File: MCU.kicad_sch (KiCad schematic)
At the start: 44 parts, among them SW201 RKB2SJM250SMTR LFS, SW202 RKB2SJM250SMTR LFS, U201 STM32F411RETx, Y201 24MHz

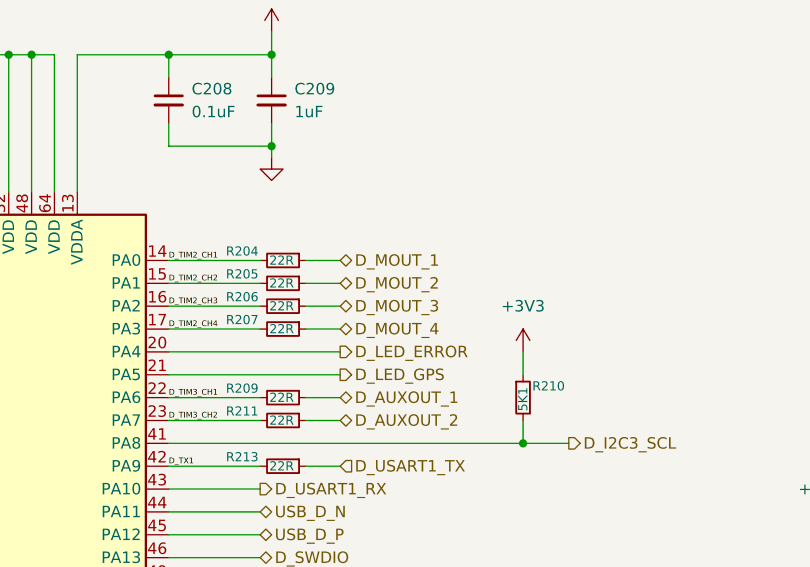
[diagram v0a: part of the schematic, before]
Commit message: fix: repositioned R24 - R206 & add silk screen for 5V input
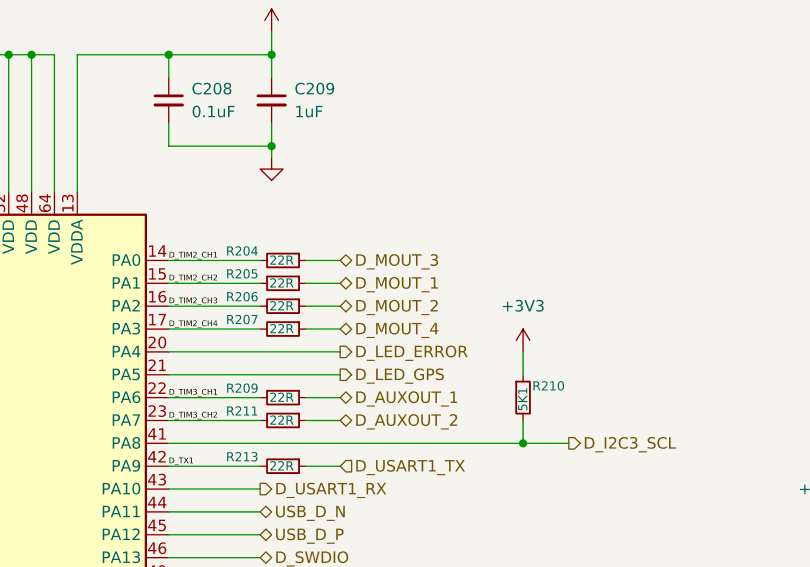
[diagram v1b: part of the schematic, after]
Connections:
- net D_MOUT_1: now also R205.1; no longer R204.1
- net D_MOUT_2: now also R206.1; no longer R205.1
- net D_MOUT_3: now also R204.1; no longer R206.1
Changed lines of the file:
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@@
 	(hierarchical_label "D_MOUT_2"
 		(shape bidirectional)
-		(at 182.88 72.39 0)
+		(at 182.88 74.93 0)
 		(effects
 			(font
@@
 	(hierarchical_label "D_MOUT_3"
 		(shape bidirectional)
-		(at 182.88 74.93 0)
+		(at 182.88 69.85 0)
 		(effects
 			(font
@@
 	(hierarchical_label "D_MOUT_1"
 		(shape bidirectional)
-		(at 182.88 69.85 0)
-		(effects
-			(font
+		(at 182.88 72.39 0)
+		(effects
+			(font

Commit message: fix: fix magnetometer pinout
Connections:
- net D_I2C1_SCL: now also U201.58 (PB6); no longer U201.61 (PB8)
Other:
- moved on the sheet: R221, R222
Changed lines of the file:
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@@
 	(title_block
 		(title "Udayate")
-		(date "2025-08-24")
-		(rev "1")
+		(date "2025-10-04")
+		(rev "1.1")
 		(comment 2 "LICENSE: CERN-OHL-S-2.0")
 		(comment 3 "GitHub: https://github.com/Ozonised/Udayate")
@@
 	)
 	(junction
-		(at 207.01 133.35)
+		(at 113.03 146.05)
 		(diameter 0)
 		(color 0 0 0 0)
 	)
 	(junction
-		(at 113.03 146.05)
+		(at 86.36 46.99)
 		(diameter 0)
 		(color 0 0 0 0)
 	)
 	(junction
-		(at 86.36 46.99)
+		(at 53.34 69.85)
 		(diameter 0)
 		(color 0 0 0 0)
 	)
 	(junction
-		(at 53.34 69.85)
+		(at 207.01 128.27)
 		(diameter 0)
 		(color 0 0 0 0)
@@
 	)
 	(junction
-		(at 210.82 120.65)
+		(at 210.82 118.11)
 		(diameter 0)
 		(color 0 0 0 0)
@@
 	)
 	(no_connect
-		(at 163.83 128.27)
-	)
-	(no_connect
 		(at 163.83 123.19)
 	)
@@
 	)
 	(no_connect
+		(at 163.83 133.35)
+	)
+	(no_connect
 		(at 128.27 87.63)
 	)
@@
 	(wire
 		(pts
-			(xy 214.63 123.19) (xy 214.63 120.65)
+			(xy 214.63 120.65) (xy 214.63 118.11)
 		)
 		(stroke
@@
 	(wire
 		(pts
-			(xy 210.82 120.65) (xy 214.63 120.65)
+			(xy 210.82 118.11) (xy 214.63 118.11)
 		)
 		(stroke
@@
 	(wire
 		(pts
-			(xy 214.63 128.27) (xy 214.63 130.81)
+			(xy 214.63 125.73) (xy 214.63 130.81)
 		)
 		(stroke
@@
 	(wire
 		(pts
-			(xy 210.82 119.38) (xy 210.82 120.65)
+			(xy 210.82 116.84) (xy 210.82 118.11)
 		)
 		(stroke
@@
 	(wire
 		(pts
-			(xy 163.83 82.55) (xy 182.88 82.55)
-		)
-		(stroke
-			(width 0)
-			(type default)
-		)
-	)
-	(wire
-		(pts
-			(xy 97.79 57.15) (xy 109.22 57.15)
+			(xy 163.83 128.27) (xy 207.01 128.27)
 		)
 		(stroke
@@
 	(wire
 		(pts
-			(xy 163.83 46.99) (xy 175.26 46.99)
+			(xy 163.83 82.55) (xy 182.88 82.55)
 		)
 		(stroke
@@
 	(wire
 		(pts
-			(xy 92.71 80.01) (xy 92.71 82.55)
+			(xy 97.79 57.15) (xy 109.22 57.15)
 		)
 		(stroke
@@
 	(wire
 		(pts
-			(xy 207.01 133.35) (xy 218.44 133.35)
+			(xy 163.83 46.99) (xy 175.26 46.99)
 		)
 		(stroke
@@
 	(wire
 		(pts
-			(xy 163.83 133.35) (xy 207.01 133.35)
+			(xy 92.71 80.01) (xy 92.71 82.55)
 		)
 		(stroke
@@
 	(wire
 		(pts
+			(xy 207.01 128.27) (xy 218.44 128.27)
+		)
+		(stroke
+			(width 0)
+			(type default)
+		)
+	)
+	(wire
+		(pts
 			(xy 203.2 87.63) (xy 203.2 90.17)
 		)
@@
 	(wire
 		(pts
-			(xy 207.01 120.65) (xy 207.01 123.19)
+			(xy 207.01 118.11) (xy 207.01 120.65)
 		)
 		(stroke
@@
 	(wire
 		(pts
-			(xy 163.83 72.39) (xy 173.99 72.39)
+			(xy 207.01 125.73) (xy 207.01 128.27)
 		)
 		(stroke
@@
 	(wire
 		(pts
-			(xy 121.92 118.11) (xy 128.27 118.11)
+			(xy 163.83 72.39) (xy 173.99 72.39)
 		)
 		(stroke
@@
 	(wire
 		(pts
-			(xy 99.06 87.63) (xy 104.14 87.63)
+			(xy 121.92 118.11) (xy 128.27 118.11)
 		)
 		(stroke
@@
 	(wire
 		(pts
-			(xy 153.67 46.99) (xy 153.67 62.23)
+			(xy 99.06 87.63) (xy 104.14 87.63)
 		)
 		(stroke
@@
 	(wire
 		(pts
-			(xy 113.03 146.05) (xy 118.11 146.05)
+			(xy 153.67 46.99) (xy 153.67 62.23)
 		)
 		(stroke
@@
 	(wire
 		(pts
-			(xy 207.01 128.27) (xy 207.01 133.35)
+			(xy 113.03 146.05) (xy 118.11 146.05)
 		)
 		(stroke
@@
 	(wire
 		(pts
-			(xy 207.01 120.65) (xy 210.82 120.65)
+			(xy 207.01 118.11) (xy 210.82 118.11)
 		)
 		(stroke
@@
 	(hierarchical_label "D_I2C1_SCL"
 		(shape output)
-		(at 218.44 133.35 0)
+		(at 218.44 128.27 0)
 		(effects
 			(font
@@
 	(symbol
 		(lib_id "power:+3V3")
-		(at 210.82 119.38 0)
+		(at 210.82 116.84 0)
 		(unit 1)
 		(exclude_from_sim no)
@@
 		(dnp no)
 		(property "Reference" "#PWR0214"
-			(at 210.82 123.19 0)
+			(at 210.82 120.65 0)
 			(effects
 				(font
@@
 		)
 		(property "Value" "+3V3"
-			(at 210.058 115.57 0)
+			(at 210.058 113.03 0)
 			(effects
 				(font
@@
 		)
 		(property "Footprint" ""
-			(at 210.82 119.38 0)
+			(at 210.82 116.84 0)
 			(effects
 				(font
@@
 		)
 		(property "Datasheet" ""
-			(at 210.82 119.38 0)
+			(at 210.82 116.84 0)
 			(effects
 				(font
@@
 		)
 		(property "Description" "Power symbol creates a global label with name \"+3V3\""
-			(at 210.82 119.38 0)
+			(at 210.82 116.84 0)
 			(effects
 				(font
@@
 	(symbol
 		(lib_id "Device:R_Small")
-		(at 214.63 125.73 0)
+		(at 214.63 123.19 0)
 		(unit 1)
 		(exclude_from_sim no)
@@
 		(dnp no)
 		(property "Reference" "R222"
-			(at 215.646 124.46 0)
+			(at 215.646 121.92 0)
 			(effects
 				(font
@@
 		)
 		(property "Value" "5K1"
-			(at 214.63 127.254 90)
+			(at 214.63 124.714 90)
 			(effects
 				(font
@@
 		)
 		(property "Footprint" "Resistor_SMD:R_0603_1608Metric_Pad0.98x0.95mm_HandSolder"
-			(at 214.63 125.73 0)
+			(at 214.63 123.19 0)
 			(effects
 				(font
@@
 		)
 		(property "Datasheet" "~"
-			(at 214.63 125.73 0)
+			(at 214.63 123.19 0)
 			(effects
 				(font
@@
 		)
 		(property "Description" "Resistor, small symbol"
-			(at 214.63 125.73 0)
+			(at 214.63 123.19 0)
 			(effects
 				(font
@@
 		)
 		(property "MPN" "CR0603-FX-5101ELF"
-			(at 214.63 125.73 0)
+			(at 214.63 123.19 0)
 			(effects
 				(font
@@
 		)
 		(property "Manufacturer" "Bourns"
-			(at 214.63 125.73 0)
+			(at 214.63 123.19 0)
 			(effects
 				(font
@@
 	(symbol
 		(lib_id "Device:R_Small")
-		(at 207.01 125.73 0)
+		(at 207.01 123.19 0)
 		(unit 1)
 		(exclude_from_sim no)
@@
 		(dnp no)
 		(property "Reference" "R221"
-			(at 208.026 124.46 0)
+			(at 208.026 121.92 0)
 			(effects
 				(font
@@
 		)
 		(property "Value" "5K1"
-			(at 207.01 127.254 90)
+			(at 207.01 124.714 90)
 			(effects
 				(font
@@
 		)
 		(property "Footprint" "Resistor_SMD:R_0603_1608Metric_Pad0.98x0.95mm_HandSolder"
-			(at 207.01 125.73 0)
+			(at 207.01 123.19 0)
 			(effects
 				(font
@@
 		)
 		(property "Datasheet" "~"
-			(at 207.01 125.73 0)
+			(at 207.01 123.19 0)
 			(effects
 				(font
@@
 		)
 		(property "Description" "Resistor, small symbol"
-			(at 207.01 125.73 0)
+			(at 207.01 123.19 0)
 			(effects
 				(font
@@
 		)
 		(property "MPN" "CR0603-FX-5101ELF"
-			(at 207.01 125.73 0)
+			(at 207.01 123.19 0)
 			(effects
 				(font
@@
 		)
 		(property "Manufacturer" "Bourns"
-			(at 207.01 125.73 0)
+			(at 207.01 123.19 0)
 			(effects
 				(font

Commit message: fix: EEPROM WC assigned to PC25
boot1 pull down, DFU now works
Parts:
- added R226: 5K1, Resistor_SMD:R_0603_1608Metric_Pad0.98x0.95mm_HandSolder, symbol Device:R_Small
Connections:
- net D_M24C02_WC: now also U201.25 (PC5); no longer U201.28 (PB2)
- net GND: now also R226.2
- new net D_BOOT1: R226.1, U201.28 (PB2)
- no-connect marks 15 -> 14
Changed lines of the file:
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@@
 	)
 	(no_connect
-		(at 128.27 105.41)
-	)
-	(no_connect
 		(at 128.27 100.33)
 	)
@@
 	(wire
 		(pts
+			(xy 208.28 104.14) (xy 208.28 105.41)
+		)
+		(stroke
+			(width 0)
+			(type default)
+		)
+	)
+	(wire
+		(pts
 			(xy 109.22 54.61) (xy 109.22 57.15)
 		)
@@
 	(wire
 		(pts
+			(xy 124.46 105.41) (xy 128.27 105.41)
+		)
+		(stroke
+			(width 0)
+			(type default)
+		)
+	)
+	(wire
+		(pts
 			(xy 210.82 118.11) (xy 214.63 118.11)
 		)
@@
 	(wire
 		(pts
+			(xy 196.85 104.14) (xy 200.66 104.14)
+		)
+		(stroke
+			(width 0)
+			(type default)
+		)
+	)
+	(wire
+		(pts
 			(xy 210.82 116.84) (xy 210.82 118.11)
 		)
@@
 	(wire
 		(pts
+			(xy 196.85 104.14) (xy 196.85 118.11)
+		)
+		(stroke
+			(width 0)
+			(type default)
+		)
+	)
+	(wire
+		(pts
 			(xy 104.14 86.36) (xy 104.14 87.63)
 		)
@@
 	(wire
 		(pts
-			(xy 163.83 118.11) (xy 181.61 118.11)
-		)
-		(stroke
-			(width 0)
-			(type default)
-		)
-	)
-	(wire
-		(pts
 			(xy 163.83 140.97) (xy 185.42 140.97)
 		)
@@
 	(wire
 		(pts
+			(xy 205.74 104.14) (xy 208.28 104.14)
+		)
+		(stroke
+			(width 0)
+			(type default)
+		)
+	)
+	(wire
+		(pts
 			(xy 87.63 121.92) (xy 92.71 121.92)
 		)
@@
 	(wire
 		(pts
+			(xy 163.83 118.11) (xy 196.85 118.11)
+		)
+		(stroke
+			(width 0)
+			(type default)
+		)
+	)
+	(wire
+		(pts
 			(xy 147.32 158.75) (xy 147.32 160.02)
 		)
@@
 		)
 	)
+	(label "D_BOOT1"
+		(at 163.83 118.11 0)
+		(effects
+			(font
+				(size 0.635 0.635)
+			)
+			(justify left bottom)
+		)
+	)
 	(label "D_R_SCK"
 		(at 163.83 143.51 0)
@@
 	(hierarchical_label "D_M24C02_WC"
 		(shape output)
-		(at 181.61 118.11 0)
+		(at 124.46 105.41 180)
 		(effects
 			(font
 				(size 1.27 1.27)
 			)
-			(justify left)
+			(justify right)
 		)
 	)
@@
 	)
 	(symbol
+		(lib_id "Device:R_Small")
+		(at 203.2 104.14 90)
+		(unit 1)
+		(exclude_from_sim no)
+		(in_bom yes)
+		(on_board yes)
+		(dnp no)
+		(property "Reference" "R226"
+			(at 200.66 103.124 90)
+			(effects
+				(font
+					(size 1.016 1.016)
+				)
+				(justify left)
+			)
+		)
+		(property "Value" "5K1"
+			(at 204.724 104.14 90)
+			(effects
+				(font
+					(size 1.016 1.016)
+				)
+				(justify left)
+			)
+		)
+		(property "Footprint" "Resistor_SMD:R_0603_1608Metric_Pad0.98x0.95mm_HandSolder"
+			(at 203.2 104.14 0)
+			(effects
+				(font
+					(size 1.27 1.27)
+				)
+				(hide yes)
+			)
+		)
+		(property "Datasheet" "~"
+			(at 203.2 104.14 0)
+			(effects
+				(font
+					(size 1.27 1.27)
+				)
+				(hide yes)
+			)
+		)
+		(property "Description" "Resistor, small symbol"
+			(at 203.2 104.14 0)
+			(effects
+				(font
+					(size 1.27 1.27)
+				)
+				(hide yes)
+			)
+		)
+		(property "MPN" "CR0603-FX-5101ELF"
+			(at 203.2 104.14 0)
+			(effects
+				(font
+					(size 1.27 1.27)
+				)
+				(hide yes)
+			)
+		)
+		(property "Manufacturer" "Bourns"
+			(at 203.2 104.14 0)
+			(effects
+				(font
+					(size 1.27 1.27)
+				)
+				(hide yes)
+			)
+		)
+		(pin "1"
+		)
+		(pin "2"
+		)
+		(instances
+			(project "Udayate"
+				(path "/855cf64b-a607-4748-8dd3-e8cd15e2a17e/e91f537f-c07e-475d-93bf-dcac5802ba81"
+					(reference "R226")
+					(unit 1)
+				)
+			)
+		)
+	)
+	(symbol
 		(lib_id "Device:C_Small")
 		(at 163.83 52.07 0)
@@
 					(unit 1)
 				)
+			)
+		)
+	)
+	(symbol
+		(lib_id "power:GND")
+		(at 208.28 105.41 0)
+		(unit 1)
+		(exclude_from_sim no)
+		(in_bom yes)
+		(on_board yes)
+		(dnp no)
+		(fields_autoplaced yes)
+		(property "Reference" "#PWR0218"
+			(at 208.28 111.76 0)
+			(effects
+				(font
+					(size 1.27 1.27)
+				)
+				(hide yes)
+			)
+		)
+		(property "Value" "GND"
+			(at 208.28 110.49 0)
+			(effects
+				(font
+					(size 1.27 1.27)
+				)
+				(hide yes)
+			)
+		)
+		(property "Footprint" ""
+			(at 208.28 105.41 0)
+			(effects
+				(font
+					(size 1.27 1.27)
+				)
+				(hide yes)
+			)
+		)
+		(property "Datasheet" ""
+			(at 208.28 105.41 0)
+			(effects
+				(font
+					(size 1.27 1.27)
+				)
+				(hide yes)
+			)
+		)
+		(property "Description" "Power symbol creates a global label with name \"GND\" , ground"
+			(at 208.28 105.41 0)
+			(effects
+				(font
+					(size 1.27 1.27)
+				)
+				(hide yes)
+			)
+		)
+		(pin "1"
+		)
+		(instances
+			(project "Udayate"
+				(path "/855cf64b-a607-4748-8dd3-e8cd15e2a17e/e91f537f-c07e-475d-93bf-dcac5802ba81"
+					(reference "#PWR0218")
+					(unit 1)
+				)
